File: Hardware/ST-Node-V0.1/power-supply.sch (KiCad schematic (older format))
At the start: 44 parts, among them Q1 SI2323DS, U1 TPS22917DBV, U2 RP605Z283B, U3 TPS22917DBV, U4 TPS22917DBV

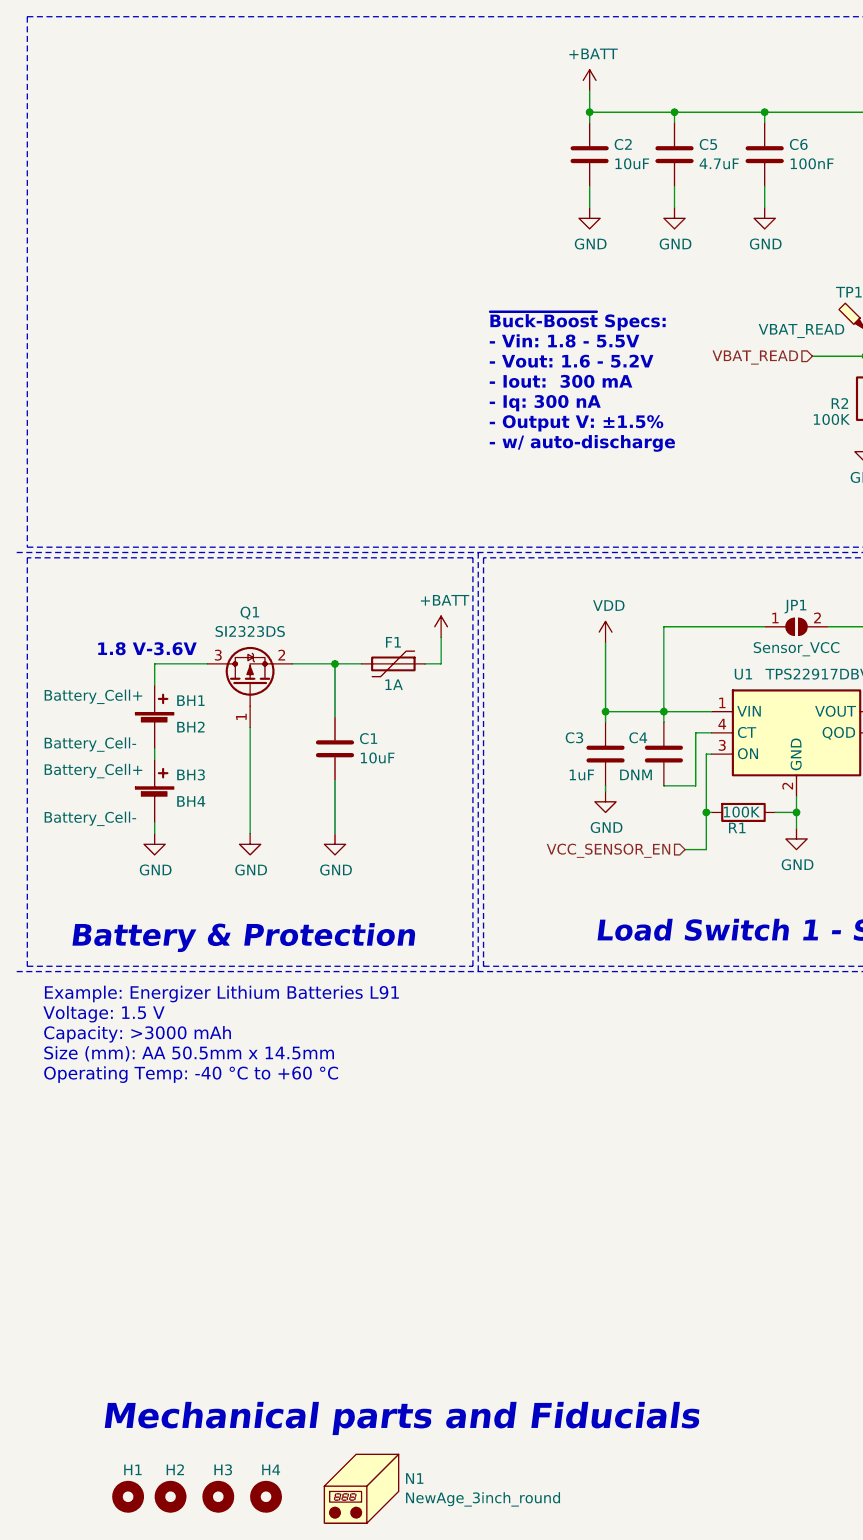
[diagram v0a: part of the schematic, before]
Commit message: sch:  Swap couple of pins and fix a HW bug
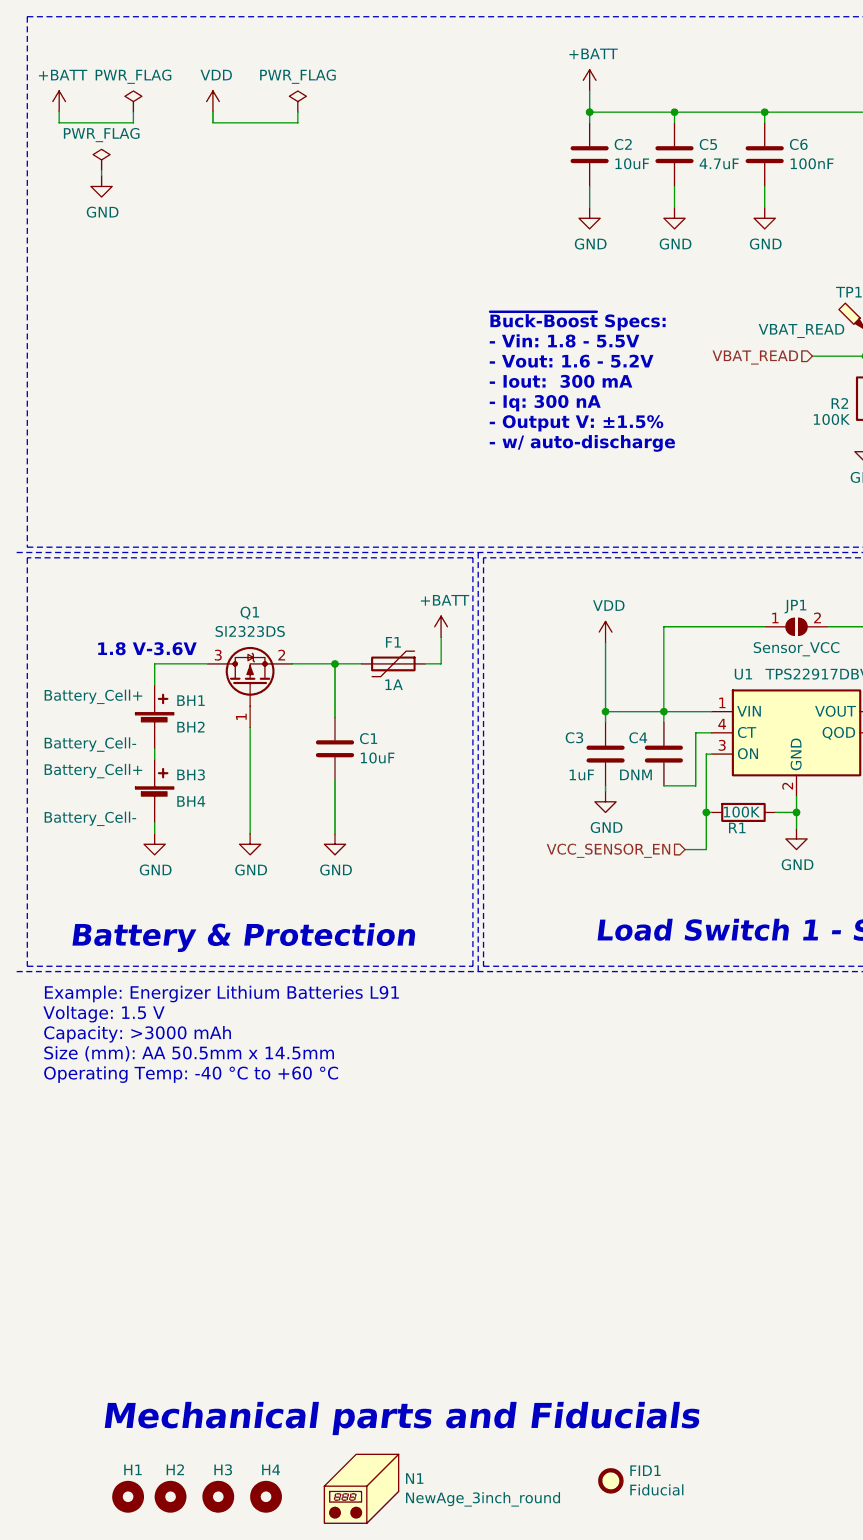
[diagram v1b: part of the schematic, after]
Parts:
- added FID1: Fiducial, Fiducial:Fiducial_0.5mm_Mask1.5mm, symbol Mechanical:Fiducial
- L1: footprint (none) -> Inductor_SMD:L_1008_2520Metric
- U2: footprint (none) -> node-lib-v1:WLCSP-20-P3_1.994x1.609mm_Layout5x4_P0.4mm
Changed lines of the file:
@@
 F 0 "U2" H 5750 1255 50  0000 C CNN
 F 1 "RP605Z283B" H 5750 1157 59  0000 C CNB
-F 2 "" H 5200 575 50  0001 L BNN
-F 3 "Ricoh" H 5200 475 50  0001 L BNN
+F 2 "node-lib-v1:WLCSP-20-P3_1.994x1.609mm_Layout5x4_P0.4mm" H 5200 575 50  0001 L BNN
+F 3 "Texas Instruments" H 5200 475 50  0001 L BNN
 F 4 "RP605Z283B-E2-F" H 5200 975 50  0001 C CNN "MPN"
 	1    5200 975
@@
 F 0 "L1" H 7128 1271 50  0000 L CNN
 F 1 "2.2 uH" H 7128 1180 50  0000 L CNN
-F 2 "" H 7075 1225 50  0001 C CNN
+F 2 "Inductor_SMD:L_1008_2520Metric" H 7075 1225 50  0001 C CNN
 F 3 "~" H 7075 1225 50  0001 C CNN
 F 4 "MLP2520H2R2ST0S1" H 7075 1225 50  0001 C CNN "MPN"
@@
 	1    0    0    -1
 $EndComp
+$Comp
+L Mechanical:Fiducial FID1
+U 1 1 5EE55870
+P 3275 7425
+F 0 "FID1" H 3360 7471 50  0000 L CNN
+F 1 "Fiducial" H 3360 7380 50  0000 L CNN
+F 2 "Fiducial:Fiducial_0.5mm_Mask1.5mm" H 3275 7425 50  0001 C CNN
+F 3 "~" H 3275 7425 50  0001 C CNN
+	1    3275 7425
+	1    0    0    -1
+$EndComp
+$Comp
+L power:GND #PWR0101
+U 1 1 5F01C425
+P 875 1275
+F 0 "#PWR0101" H 875 1025 50  0001 C CNN
+F 1 "GND" H 880 1102 50  0000 C CNN
+F 2 "" H 875 1275 50  0001 C CNN
+F 3 "" H 875 1275 50  0001 C CNN
+	1    875  1275
+	1    0    0    -1
+$EndComp
+$Comp
+L power:PWR_FLAG #FLG0101
+U 1 1 5F01C740
+P 1025 975
+F 0 "#FLG0101" H 1025 1050 50  0001 C CNN
+F 1 "PWR_FLAG" H 1025 1148 50  0000 C CNN
+F 2 "" H 1025 975 50  0001 C CNN
+F 3 "~" H 1025 975 50  0001 C CNN
+	1    1025 975
+	1    0    0    -1
+$EndComp
+$Comp
+L power:+BATT #PWR0102
+U 1 1 5F01CCBE
+P 675 975
+F 0 "#PWR0102" H 675 825 50  0001 C CNN
+F 1 "+BATT" H 690 1148 50  0000 C CNN
+F 2 "" H 675 975 50  0001 C CNN
+F 3 "" H 675 975 50  0001 C CNN
+	1    675  975
+	1    0    0    -1
+$EndComp
+Wire Wire Line
+	675  975  675  1025
+Wire Wire Line
+	675  1025 1025 1025
+Wire Wire Line
+	1025 1025 1025 975
+$Comp
+L power:PWR_FLAG #FLG0103
+U 1 1 5F023D29
+P 875 1250
+F 0 "#FLG0103" H 875 1325 50  0001 C CNN
+F 1 "PWR_FLAG" H 875 1423 50  0000 C CNN
+F 2 "" H 875 1250 50  0001 C CNN
+F 3 "~" H 875 1250 50  0001 C CNN
+	1    875  1250
+	1    0    0    -1
+$EndComp
+Wire Wire Line
+	875  1250 875  1275
+$Comp
+L power:VDD #PWR0103
+U 1 1 5F03306D
+P 1400 975
+F 0 "#PWR0103" H 1400 825 50  0001 C CNN
+F 1 "VDD" H 1417 1148 50  0000 C CNN
+F 2 "" H 1400 975 50  0001 C CNN
+F 3 "" H 1400 975 50  0001 C CNN
+	1    1400 975
+	1    0    0    -1
+$EndComp
+$Comp
+L power:PWR_FLAG #FLG0104
+U 1 1 5F033A93
+P 1800 975
+F 0 "#FLG0104" H 1800 1050 50  0001 C CNN
+F 1 "PWR_FLAG" H 1800 1148 50  0000 C CNN
+F 2 "" H 1800 975 50  0001 C CNN
+F 3 "~" H 1800 975 50  0001 C CNN
+	1    1800 975
+	1    0    0    -1
+$EndComp
+Wire Wire Line
+	1400 975  1400 1025
+Wire Wire Line
+	1400 1025 1800 1025
+Wire Wire Line
+	1800 1025 1800 975
 $EndSCHEMATC

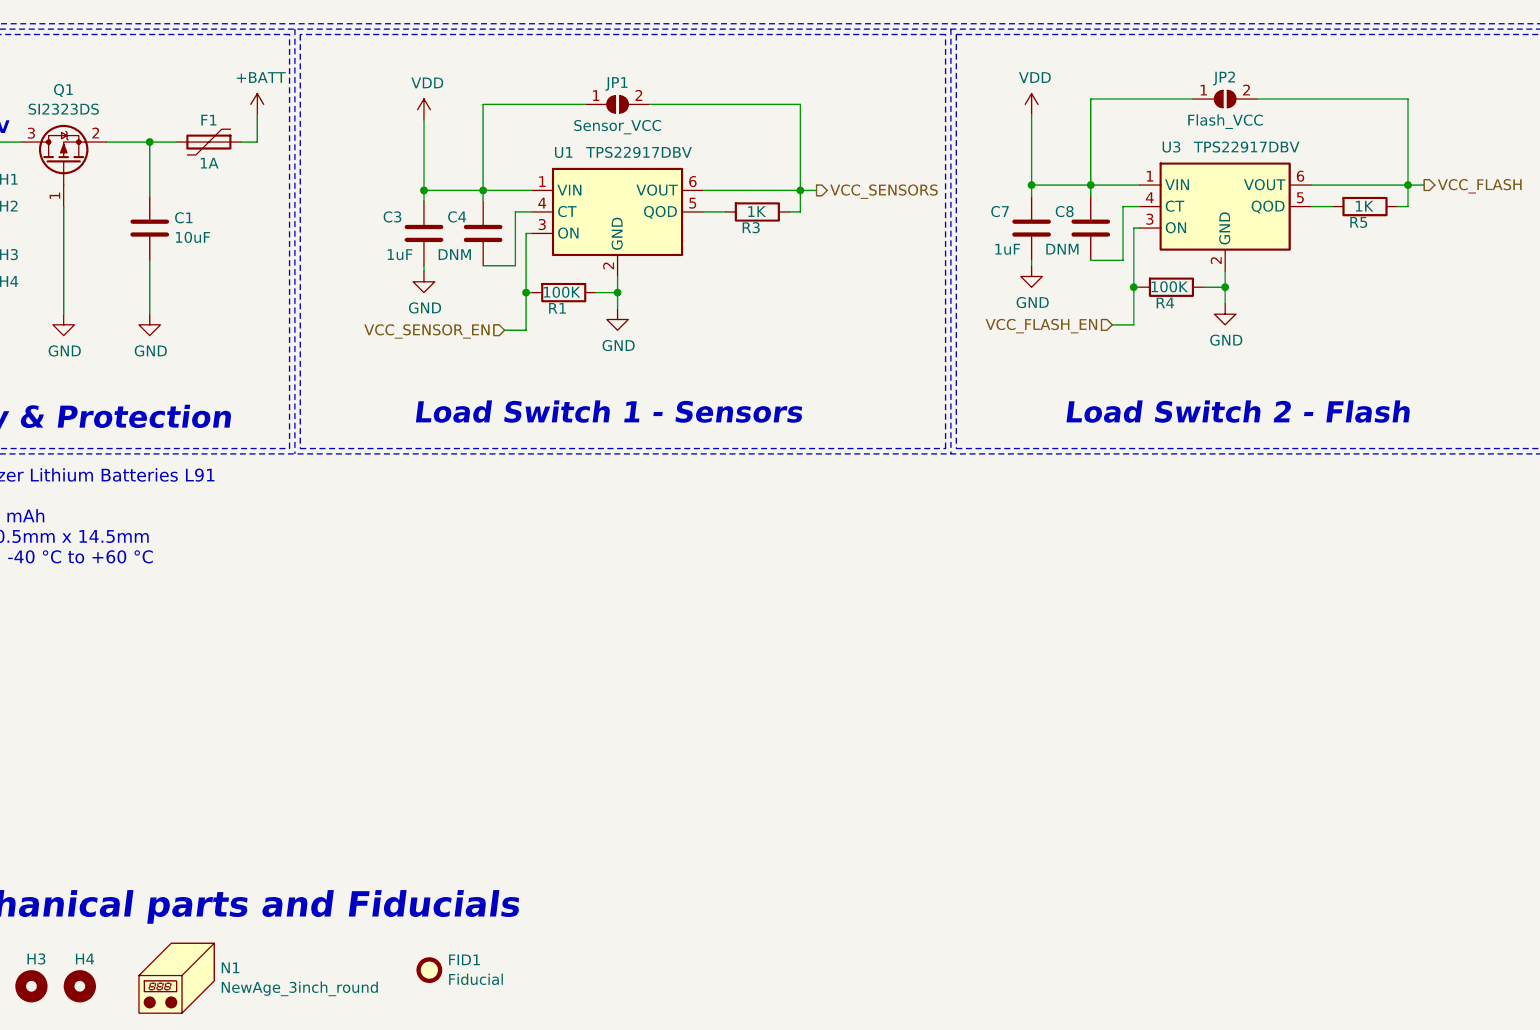
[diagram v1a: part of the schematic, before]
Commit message: sch, pcb: Improve pcb layout, swap sch pins
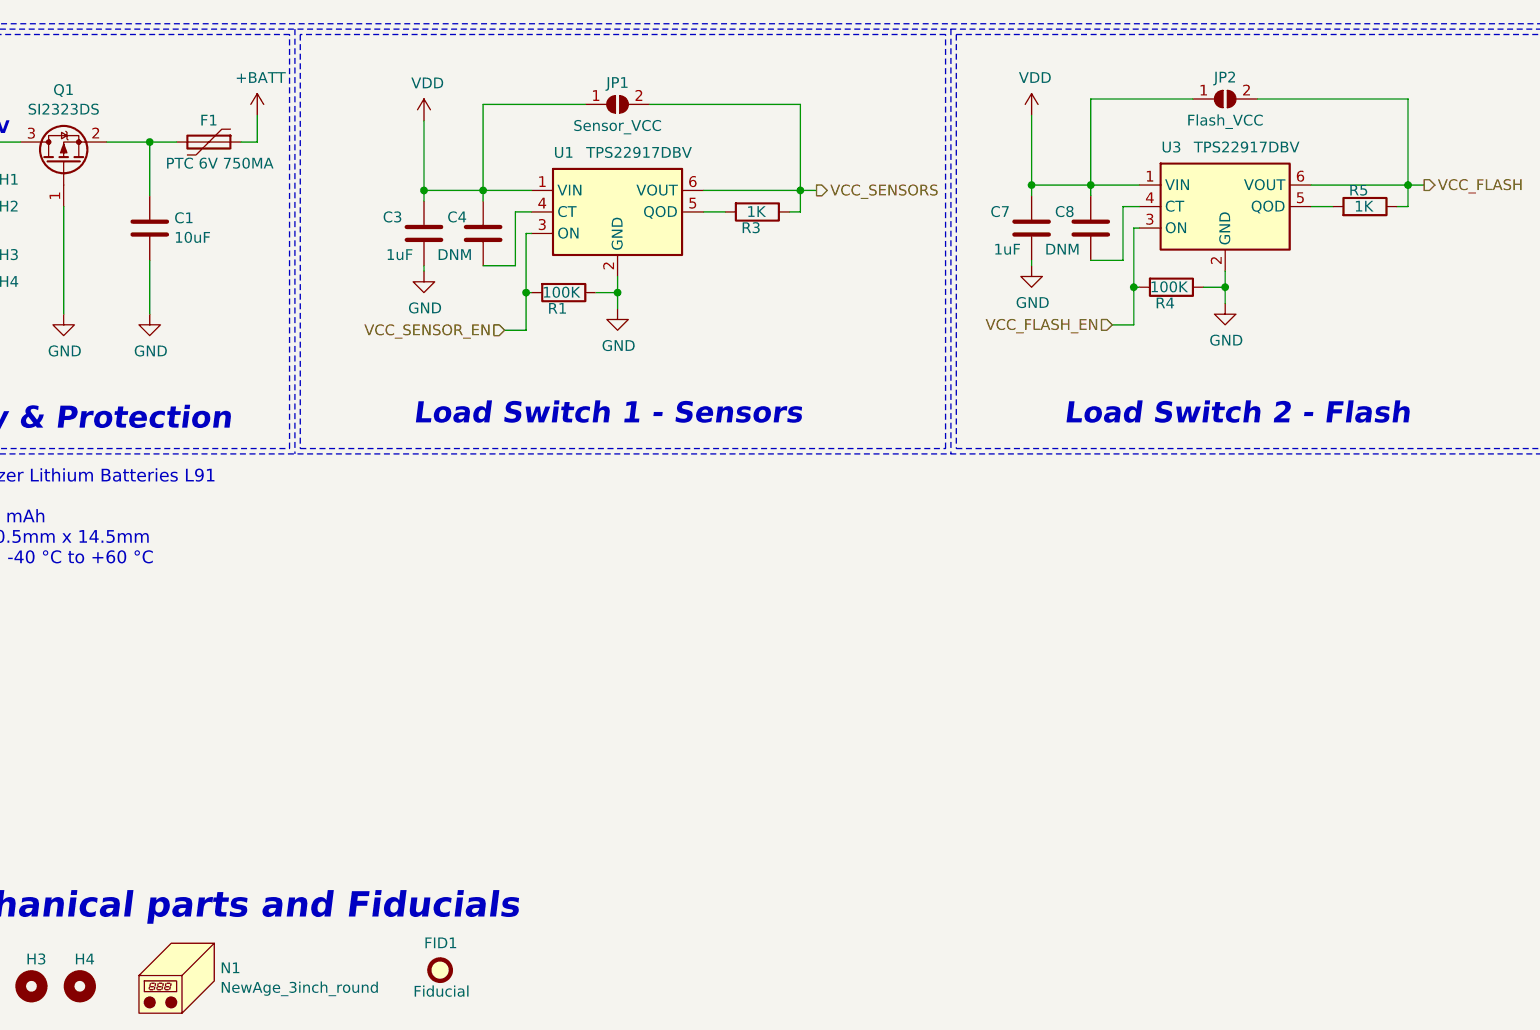
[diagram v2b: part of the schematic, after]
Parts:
- C1, C2: MPN GRM155R60J106M -> C1608X5R0J106K080AB
- C10: MPN GRM155R60J106M -> (none)
- C12, C3, C7: MPN (none) -> CL05A105KQ5NNNC
- C5: MPN (none) -> C1608X5R1C475K080AC
- C6: MPN GRM155R61A104K -> CC0402KRX7R7BB104
- C9: MPN (none) -> CC0402KRX7R7BB104
- F1: value 1A -> PTC 6V 750MA; footprint Fuse:Fuse_0603_1608Metric -> node-lib-v1:Fuse_0805_2012Metric_Castellated; MPN (none) -> 0ZCK0075FF2E
- JP1, JP2, JP3: footprint Jumper:SolderJumper-2_P1.3mm_Open_TrianglePad1.0x1.5mm -> Jumper:SolderJumper-2_P1.3mm_Open_RoundedPad1.0x1.5mm
- L1: MPN MLP2520H2R2ST0S1 -> CVH252009-2R2M
- N1: MPN (none) -> S6L-303013
- R1, R2, R4, R7: MPN (none) -> RC0402FR-07100KL
- R3, R5, R8: MPN (none) -> RC0402FR-071KP
- R6: MPN (none) -> RC0402FR-070RL
- U1, U3, U4: MPN (none) -> TPS22917DBVR
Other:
- moved on the sheet: FID1
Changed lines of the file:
@@
 P 2250 3575
 F 0 "F1" V 2150 3575 50  0000 C CNN
-F 1 "1A" V 2350 3575 50  0000 C CNN
-F 2 "Fuse:Fuse_0603_1608Metric" H 2300 3375 50  0001 L CNN
+F 1 "PTC 6V 750MA" V 2350 3625 50  0000 C CNN
+F 2 "node-lib-v1:Fuse_0805_2012Metric_Castellated" H 2300 3375 50  0001 L CNN
 F 3 "~" H 2250 3575 50  0001 C CNN
+F 4 "0ZCK0075FF2E" V 2250 3575 50  0001 C CNN "MPN"
 	1    2250 3575
 	0    1    1    0
@@
 F 2 "Package_TO_SOT_SMD:SOT-23-6" H 4150 4400 50  0001 C CNN
 F 3 "http://www.ti.com/lit/ds/symlink/tps22917.pdf" H 4200 3200 50  0001 C CNN
+F 4 "TPS22917DBVR" H 4150 3900 50  0001 C CNN "MPN"
 	1    4150 3900
 	1    0    0    -1
@@
 F 2 "Capacitor_SMD:C_0402_1005Metric" H 7088 2175 50  0001 C CNN
 F 3 "~" H 7050 2325 50  0001 C CNN
+F 4 "CC0402KRX7R7BB104" H 7050 2325 50  0001 C CNN "MPN"
 	1    7050 2325
 	1    0    0    -1
@@
 F 2 "Capacitor_SMD:C_0603_1608Metric" H 3613 1025 50  0001 C CNN
 F 3 "~" H 3575 1175 50  0001 C CNN
+F 4 "C1608X5R1C475K080AC" H 3575 1175 50  0001 C CNN "MPN"
 	1    3575 1175
 	1    0    0    -1
@@
 F 2 "Capacitor_SMD:C_0603_1608Metric" H 3213 1025 50  0001 C CNN
 F 3 "~" H 3175 1175 50  0001 C CNN
-F 4 "GRM155R60J106M" H 3175 1175 50  0001 C CNN "MPN"
+F 4 "C1608X5R0J106K080AB" H 3175 1175 50  0001 C CNN "MPN"
 	1    3175 1175
 	-1   0    0    1
@@
 F 2 "Capacitor_SMD:C_0402_1005Metric" H 4038 1025 50  0001 C CNN
 F 3 "~" H 4000 1175 50  0001 C CNN
-F 4 "GRM155R61A104K" H 4000 1175 50  0001 C CNN "MPN"
+F 4 "CC0402KRX7R7BB104" H 4000 1175 50  0001 C CNN "MPN"
 	1    4000 1175
 	1    0    0    -1
@@
 F 2 "Resistor_SMD:R_0402_1005Metric" V 4730 3900 50  0001 C CNN
 F 3 "~" H 4800 3900 50  0001 C CNN
+F 4 "RC0402FR-071KP" H 4800 3900 50  0001 C CNN "MPN"
 	1    4800 3900
 	0    1    1    0
@@
 F 2 "Resistor_SMD:R_0402_1005Metric" V 3830 4275 50  0001 C CNN
 F 3 "~" H 3900 4275 50  0001 C CNN
+F 4 "RC0402FR-07100KL	" H 3900 4275 50  0001 C CNN "MPN"
 	1    3900 4275
 	0    1    1    0
@@
 F 2 "Capacitor_SMD:C_0402_1005Metric" H 3288 3850 50  0001 C CNN
 F 3 "~" H 3250 4000 50  0001 C CNN
+F 4 "CL05A105KQ5NNNC" H 3250 4000 50  0001 C CNN "MPN"
 	1    3250 4000
 	-1   0    0    -1
@@
 F 0 "JP1" H 4150 3500 50  0000 C CNN
 F 1 "Sensor_VCC" H 4150 3300 50  0000 C CNN
-F 2 "Jumper:SolderJumper-2_P1.3mm_Open_TrianglePad1.0x1.5mm" H 4150 3400 50  0001 C CNN
+F 2 "Jumper:SolderJumper-2_P1.3mm_Open_RoundedPad1.0x1.5mm" H 4150 3400 50  0001 C CNN
 F 3 "~" H 4150 3400 50  0001 C CNN
 	1    4150 3400
@@
 F 2 "Package_TO_SOT_SMD:SOT-23-6" H 6975 4375 50  0001 C CNN
 F 3 "http://www.ti.com/lit/ds/symlink/tps22917.pdf" H 7025 3175 50  0001 C CNN
+F 4 "TPS22917DBVR" H 6975 3875 50  0001 C CNN "MPN"
 	1    6975 3875
 	1    0    0    -1
@@
 F 2 "Resistor_SMD:R_0402_1005Metric" V 7555 3875 50  0001 C CNN
 F 3 "~" H 7625 3875 50  0001 C CNN
+F 4 "RC0402FR-071KP" H 7625 3875 50  0001 C CNN "MPN"
 	1    7625 3875
-	0    1    1    0
+	0    1    -1   0
 $EndComp
 $Comp
@@
 F 2 "Resistor_SMD:R_0402_1005Metric" V 6655 4250 50  0001 C CNN
 F 3 "~" H 6725 4250 50  0001 C CNN
+F 4 "RC0402FR-07100KL	" H 6725 4250 50  0001 C CNN "MPN"
 	1    6725 4250
 	0    1    1    0
@@
 F 2 "Capacitor_SMD:C_0402_1005Metric" H 6113 3825 50  0001 C CNN
 F 3 "~" H 6075 3975 50  0001 C CNN
+F 4 "CL05A105KQ5NNNC" H 6075 3975 50  0001 C CNN "MPN"
 	1    6075 3975
 	-1   0    0    -1
@@
 F 0 "JP2" H 6975 3475 50  0000 C CNN
 F 1 "Flash_VCC" H 6975 3275 50  0000 C CNN
-F 2 "Jumper:SolderJumper-2_P1.3mm_Open_TrianglePad1.0x1.5mm" H 6975 3375 50  0001 C CNN
+F 2 "Jumper:SolderJumper-2_P1.3mm_Open_RoundedPad1.0x1.5mm" H 6975 3375 50  0001 C CNN
 F 3 "~" H 6975 3375 50  0001 C CNN
 	1    6975 3375
@@
 F 2 "Package_TO_SOT_SMD:SOT-23-6" H 9700 4400 50  0001 C CNN
 F 3 "http://www.ti.com/lit/ds/symlink/tps22917.pdf" H 9750 3200 50  0001 C CNN
+F 4 "TPS22917DBVR" H 9700 3900 50  0001 C CNN "MPN"
 	1    9700 3900
 	1    0    0    -1
@@
 F 2 "Resistor_SMD:R_0402_1005Metric" V 10280 3900 50  0001 C CNN
 F 3 "~" H 10350 3900 50  0001 C CNN
+F 4 "RC0402FR-071KP" H 10350 3900 50  0001 C CNN "MPN"
 	1    10350 3900
 	0    1    1    0
@@
 F 2 "Resistor_SMD:R_0402_1005Metric" V 9380 4275 50  0001 C CNN
 F 3 "~" H 9450 4275 50  0001 C CNN
+F 4 "RC0402FR-07100KL	" H 9450 4275 50  0001 C CNN "MPN"
 	1    9450 4275
 	0    1    1    0
@@
 F 2 "Capacitor_SMD:C_0402_1005Metric" H 8838 3850 50  0001 C CNN
 F 3 "~" H 8800 4000 50  0001 C CNN
+F 4 "CL05A105KQ5NNNC" H 8800 4000 50  0001 C CNN "MPN"
 	1    8800 4000
 	-1   0    0    -1
@@
 F 0 "JP3" H 9700 3500 50  0000 C CNN
 F 1 "Secure_Element_VCC" H 9700 3300 50  0000 C CNN
-F 2 "Jumper:SolderJumper-2_P1.3mm_Open_TrianglePad1.0x1.5mm" H 9700 3400 50  0001 C CNN
+F 2 "Jumper:SolderJumper-2_P1.3mm_Open_RoundedPad1.0x1.5mm" H 9700 3400 50  0001 C CNN
 F 3 "~" H 9700 3400 50  0001 C CNN
 	1    9700 3400
@@
 F 2 "node-lib-v1:NewAge_3inch_round" H 2200 7500 50  0001 C CNN
 F 3 "~" H 2200 7500 50  0001 C CNN
+F 4 "S6L-303013" H 2150 7450 50  0001 C CNN "MPN"
 	1    2150 7450
 	1    0    0    -1
@@
 F 2 "Resistor_SMD:R_0402_1005Metric" V 4405 2325 50  0001 C CNN
 F 3 "~" H 4475 2325 50  0001 C CNN
+F 4 "RC0402FR-07100KL	" H 4475 2325 50  0001 C CNN "MPN"
 	1    4475 2325
 	-1   0    0    1
@@
 F 2 "Inductor_SMD:L_1008_2520Metric" H 7075 1225 50  0001 C CNN
 F 3 "~" H 7075 1225 50  0001 C CNN
-F 4 "MLP2520H2R2ST0S1" H 7075 1225 50  0001 C CNN "MPN"
+F 4 "CVH252009-2R2M" H 7075 1225 50  0001 C CNN "MPN"
 	1    7075 1225
 	1    0    0    -1
@@
 F 2 "Capacitor_SMD:C_0603_1608Metric" H 7788 1675 50  0001 C CNN
 F 3 "~" H 7750 1825 50  0001 C CNN
-F 4 "GRM155R60J106M" H 7750 1825 50  0001 C CNN "MPN"
+F 4 "" H 7750 1825 50  0001 C CNN "MPN"
 	1    7750 1825
 	-1   0    0    1
@@
 F 2 "Capacitor_SMD:C_0603_1608Metric" H 2013 3825 50  0001 C CNN
 F 3 "~" H 1975 3975 50  0001 C CNN
-F 4 "GRM155R60J106M" H 1975 3975 50  0001 C CNN "MPN"
+F 4 "C1608X5R0J106K080AB" H 1975 3975 50  0001 C CNN "MPN"
 	1    1975 3975
 	-1   0    0    1
@@
 F 2 "Resistor_SMD:R_0402_1005Metric" V 8480 1625 50  0001 C CNN
 F 3 "~" H 8550 1625 50  0001 C CNN
+F 4 "RC0402FR-070RL" H 8550 1625 50  0001 C CNN "MPN"
 	1    8550 1625
 	0    -1   -1   0
@@
 L Mechanical:Fiducial FID1
 U 1 1 5EE55870
-P 3275 7425
-F 0 "FID1" H 3360 7471 50  0000 L CNN
-F 1 "Fiducial" H 3360 7380 50  0000 L CNN
-F 2 "Fiducial:Fiducial_0.5mm_Mask1.5mm" H 3275 7425 50  0001 C CNN
-F 3 "~" H 3275 7425 50  0001 C CNN
-	1    3275 7425
-	1    0    0    -1
-$EndComp
+P 3325 7425
+F 0 "FID1" H 3250 7550 50  0000 L CNN
+F 1 "Fiducial" H 3200 7325 50  0000 L CNN
+F 2 "Fiducial:Fiducial_0.5mm_Mask1.5mm" H 3325 7425 50  0001 C CNN
+F 3 "~" H 3325 7425 50  0001 C CNN
+	1    3325 7425
+	1    0    0    -1
+$EndComp
